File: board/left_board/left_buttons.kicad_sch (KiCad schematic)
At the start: 17 parts, among them SW201 SW_Push, SW202 SW_Push, SW203 SW_Push, SW204 SW_Push, SW205 SW_Push, SW206 SW_Push, SW207 SW_Push, SW208 SW_Push, SW209 SW_Push, SW210 SW_Push, SW211 SW_Push, SW212 SW_Push, SW213 SW_Push

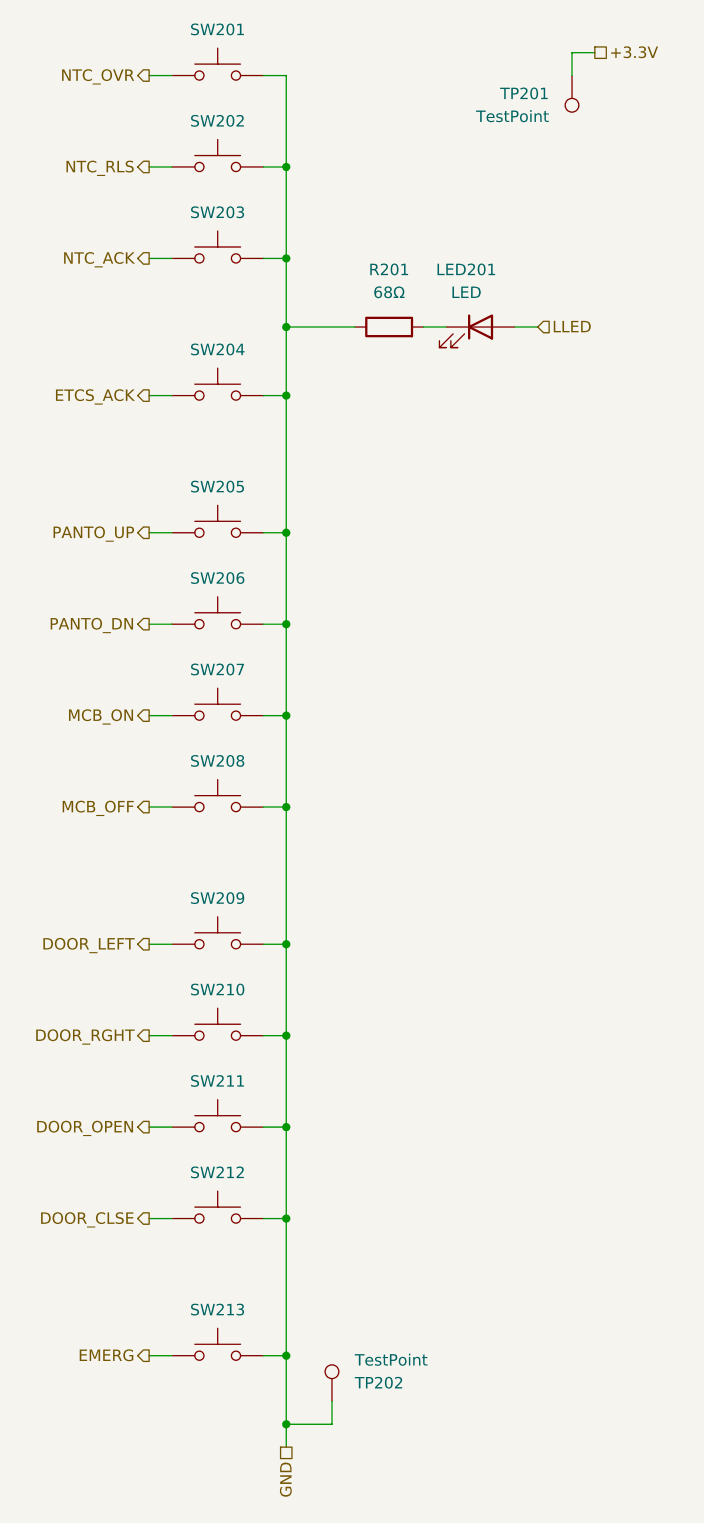
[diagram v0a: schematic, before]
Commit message: add support for pedal
the pedal is mostly envisioned as a secondary dead man's switch input, but
to enable flexible usage, it is wired up to the µC's ADC and supplies
12-bit values for the X axis

things will be set up to cooperate with a Brother-compatible sewing machine
pedal because that's what I have lying around -- those that connect using a
3.5mm TS phone connector, nothing even close to mains voltage
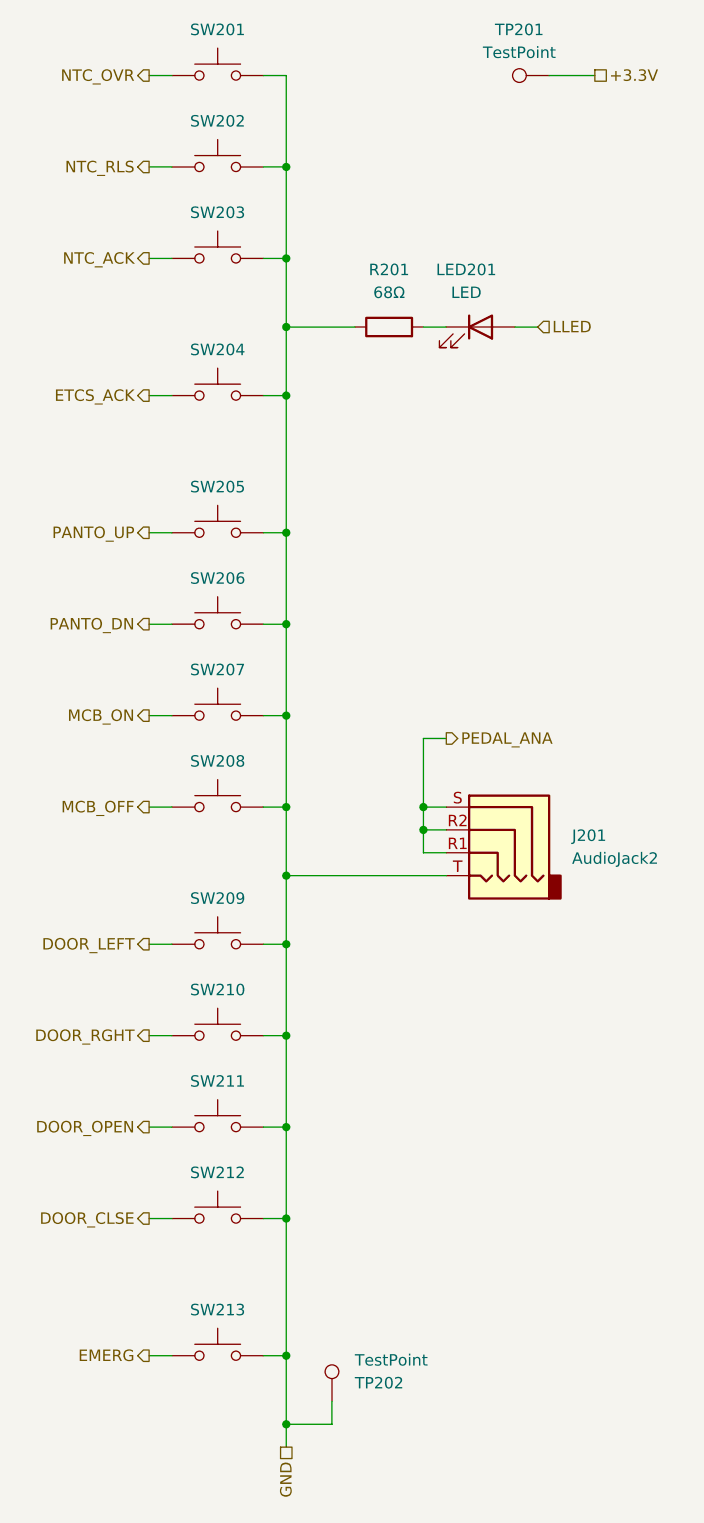
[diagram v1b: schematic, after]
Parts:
- added J201: AudioJack2, Connector_Audio:Jack_3.5mm_PJ320D_Horizontal, symbol Connector_Audio:AudioJack4
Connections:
- net GND: now also J201.T
- new net PEDAL_ANA: J201.R1, J201.R2, J201.S
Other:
- moved on the sheet: TP201
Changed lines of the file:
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@@
+	)
+	(junction
+		(at 74.93 104.14)
+		(diameter 0)
+		(color 0 0 0 0)
+	)
+	(junction
+		(at 74.93 106.68)
+		(diameter 0)
+		(color 0 0 0 0)
 	)
 	(junction
@@
 		(color 0 0 0 0)
 	)
+	(junction
+		(at 59.69 111.76)
+		(diameter 0)
+		(color 0 0 0 0)
+	)
 	(wire
 		(pts
@@
 	(wire
 		(pts
+			(xy 59.69 111.76) (xy 59.69 119.38)
+		)
+		(stroke
+			(width 0)
+			(type default)
+		)
+	)
+	(wire
+		(pts
 			(xy 59.69 22.86) (xy 59.69 33.02)
 		)
@@
 	(wire
 		(pts
+			(xy 74.93 104.14) (xy 74.93 106.68)
+		)
+		(stroke
+			(width 0)
+			(type default)
+		)
+	)
+	(wire
+		(pts
 			(xy 59.69 73.66) (xy 59.69 83.82)
 		)
@@
 	(wire
 		(pts
+			(xy 74.93 104.14) (xy 77.47 104.14)
+		)
+		(stroke
+			(width 0)
+			(type default)
+		)
+	)
+	(wire
+		(pts
 			(xy 57.15 149.86) (xy 59.69 149.86)
 		)
@@
 	(wire
 		(pts
-			(xy 91.44 20.32) (xy 91.44 22.86)
+			(xy 77.47 109.22) (xy 74.93 109.22)
+		)
+		(stroke
+			(width 0)
+			(type default)
+		)
+	)
+	(wire
+		(pts
+			(xy 88.9 22.86) (xy 93.98 22.86)
 		)
 		(stroke
@@
 	(wire
 		(pts
-			(xy 91.44 20.32) (xy 93.98 20.32)
-		)
-		(stroke
-			(width 0)
-			(type default)
-		)
-	)
-	(wire
-		(pts
 			(xy 44.45 73.66) (xy 46.99 73.66)
 		)
@@
 	(wire
 		(pts
+			(xy 74.93 96.52) (xy 77.47 96.52)
+		)
+		(stroke
+			(width 0)
+			(type default)
+		)
+	)
+	(wire
+		(pts
 			(xy 59.69 149.86) (xy 59.69 165.1)
 		)
@@
 	(wire
 		(pts
-			(xy 59.69 104.14) (xy 59.69 119.38)
+			(xy 59.69 104.14) (xy 59.69 111.76)
 		)
 		(stroke
@@
 	(wire
 		(pts
+			(xy 74.93 104.14) (xy 74.93 96.52)
+		)
+		(stroke
+			(width 0)
+			(type default)
+		)
+	)
+	(wire
+		(pts
+			(xy 74.93 106.68) (xy 77.47 106.68)
+		)
+		(stroke
+			(width 0)
+			(type default)
+		)
+	)
+	(wire
+		(pts
 			(xy 57.15 139.7) (xy 59.69 139.7)
 		)
@@
 	(wire
 		(pts
+			(xy 74.93 109.22) (xy 74.93 106.68)
+		)
+		(stroke
+			(width 0)
+			(type default)
+		)
+	)
+	(wire
+		(pts
 			(xy 57.15 58.42) (xy 59.69 58.42)
 		)
@@
 		(pts
 			(xy 59.69 58.42) (xy 59.69 73.66)
+		)
+		(stroke
+			(width 0)
+			(type default)
+		)
+	)
+	(wire
+		(pts
+			(xy 59.69 111.76) (xy 77.47 111.76)
 		)
 		(stroke
@@
 		)
 	)
+	(hierarchical_label "PEDAL_ANA"
+		(shape output)
+		(at 77.47 96.52 0)
+		(fields_autoplaced yes)
+		(effects
+			(font
+				(size 1.27 1.27)
+			)
+			(justify left)
+		)
+	)
 	(hierarchical_label "NTC_RLS"
 		(shape output)
@@
 	(hierarchical_label "+3.3V"
 		(shape passive)
-		(at 93.98 20.32 0)
+		(at 93.98 22.86 0)
 		(fields_autoplaced yes)
 		(effects
@@
 	(symbol
 		(lib_id "Connector:TestPoint")
-		(at 91.44 22.86 0)
+		(at 88.9 22.86 90)
 		(mirror x)
 		(unit 1)
@@
 		(fields_autoplaced yes)
 		(property "Reference" "TP201"
-			(at 88.9 24.8919 0)
-			(effects
-				(font
-					(size 1.27 1.27)
-				)
-				(justify right)
+			(at 85.598 17.78 90)
+			(effects
+				(font
+					(size 1.27 1.27)
+				)
 			)
 		)
 		(property "Value" "TestPoint"
-			(at 88.9 27.4319 0)
-			(effects
-				(font
-					(size 1.27 1.27)
-				)
-				(justify right)
+			(at 85.598 20.32 90)
+			(effects
+				(font
+					(size 1.27 1.27)
+				)
 			)
 		)
 		(property "Footprint" "TestPoint:TestPoint_Pad_D1.0mm"
-			(at 96.52 22.86 0)
+			(at 88.9 27.94 0)
 			(effects
 				(font
@@
 		)
 		(property "Datasheet" "~"
-			(at 96.52 22.86 0)
+			(at 88.9 27.94 0)
 			(effects
 				(font
@@
 		)
 		(property "Description" "test point"
-			(at 91.44 22.86 0)
+			(at 88.9 22.86 0)
 			(effects
 				(font
@@
 					(unit 1)
 				)
+			)
+		)
+	)
+	(symbol
+		(lib_id "Connector_Audio:AudioJack4")
+		(at 82.55 106.68 0)
+		(mirror y)
+		(unit 1)
+		(exclude_from_sim no)
+		(in_bom yes)
+		(on_board yes)
+		(dnp no)
+		(fields_autoplaced yes)
+		(property "Reference" "J201"
+			(at 91.44 107.3149 0)
+			(effects
+				(font
+					(size 1.27 1.27)
+				)
+				(justify right)
+			)
+		)
+		(property "Value" "AudioJack2"
+			(at 91.44 109.8549 0)
+			(effects
+				(font
+					(size 1.27 1.27)
+				)
+				(justify right)
+			)
+		)
+		(property "Footprint" "Connector_Audio:Jack_3.5mm_PJ320D_Horizontal"
+			(at 82.55 106.68 0)
+			(effects
+				(font
+					(size 1.27 1.27)
+				)
+				(hide yes)
+			)
+		)
+		(property "Datasheet" "~"
+			(at 82.55 106.68 0)
+			(effects
+				(font
+					(size 1.27 1.27)
+				)
+				(hide yes)
+			)
+		)
+		(property "Description" "Audio Jack, 4 Poles (TRRS)"
+			(at 82.55 106.68 0)
+			(effects
+				(font
+					(size 1.27 1.27)
+				)
+				(hide yes)
+			)
+		)
+		(property "LCSC" "C431535"
+			(at 82.55 106.68 0)
+			(effects
+				(font
+					(size 1.27 1.27)
+				)
+				(hide yes)
+			)
+		)
+		(pin "S"
+		)
+		(pin "T"
+		)
+		(pin "R2"
+		)
+		(pin "R1"
+		)
+		(instances
+			(project ""
+				(path "/781b8cf7-c5e9-458b-bc5e-9d97c21958eb/ee7ea56d-ccae-4129-b9a8-76b6e32e09cb"
+					(reference "J201")
+					(unit 1)
+				)

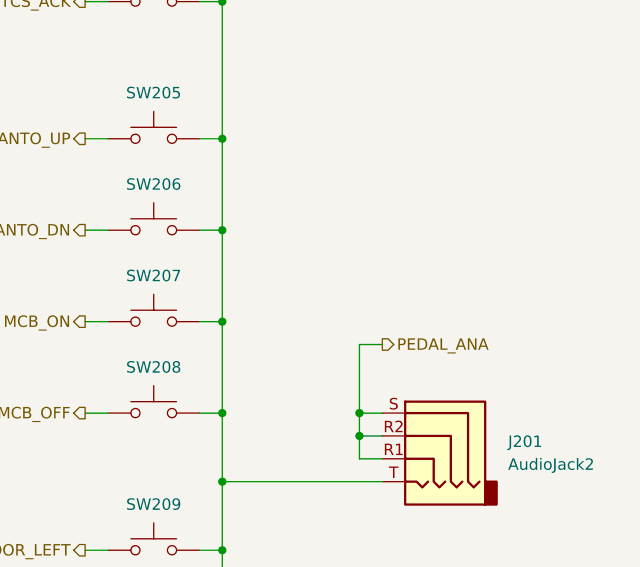
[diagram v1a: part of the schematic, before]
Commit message: left board: pullup resistor for pedal
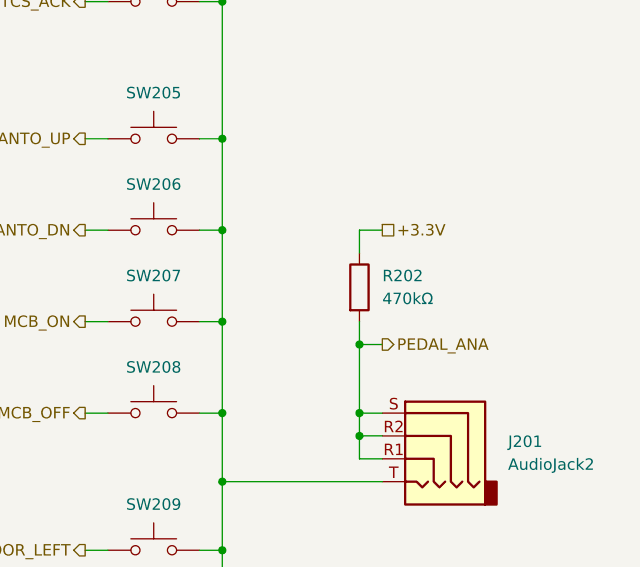
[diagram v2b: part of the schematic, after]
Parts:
- added R202: 470kΩ, Resistor_SMD:R_0603_1608Metric, symbol Device:R
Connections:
- net +3.3V: now also R202.1
- net PEDAL_ANA: now also R202.2
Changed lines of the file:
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@@
+	)
+	(junction
+		(at 74.93 96.52)
+		(diameter 0)
+		(color 0 0 0 0)
 	)
 	(junction
@@
 	(wire
 		(pts
+			(xy 74.93 93.98) (xy 74.93 96.52)
+		)
+		(stroke
+			(width 0)
+			(type default)
+		)
+	)
+	(wire
+		(pts
 			(xy 44.45 73.66) (xy 46.99 73.66)
 		)
@@
 	(wire
 		(pts
+			(xy 74.93 83.82) (xy 77.47 83.82)
+		)
+		(stroke
+			(width 0)
+			(type default)
+		)
+	)
+	(wire
+		(pts
 			(xy 59.69 149.86) (xy 59.69 165.1)
 		)
@@
 		(pts
 			(xy 44.45 33.02) (xy 46.99 33.02)
+		)
+		(stroke
+			(width 0)
+			(type default)
+		)
+	)
+	(wire
+		(pts
+			(xy 74.93 86.36) (xy 74.93 83.82)
 		)
 		(stroke
@@
 			)
 			(justify right)
+		)
+	)
+	(hierarchical_label "+3.3V"
+		(shape passive)
+		(at 77.47 83.82 0)
+		(fields_autoplaced yes)
+		(effects
+			(font
+				(size 1.27 1.27)
+			)
+			(justify left)
 		)
 	)
@@
 					(unit 1)
 				)
+			)
+		)
+	)
+	(symbol
+		(lib_id "Device:R")
+		(at 74.93 90.17 0)
+		(unit 1)
+		(exclude_from_sim no)
+		(in_bom yes)
+		(on_board yes)
+		(dnp no)
+		(fields_autoplaced yes)
+		(property "Reference" "R202"
+			(at 77.47 88.8999 0)
+			(effects
+				(font
+					(size 1.27 1.27)
+				)
+				(justify left)
+			)
+		)
+		(property "Value" "470kΩ"
+			(at 77.47 91.4399 0)
+			(effects
+				(font
+					(size 1.27 1.27)
+				)
+				(justify left)
+			)
+		)
+		(property "Footprint" "Resistor_SMD:R_0603_1608Metric"
+			(at 73.152 90.17 90)
+			(effects
+				(font
+					(size 1.27 1.27)
+				)
+				(hide yes)
+			)
+		)
+		(property "Datasheet" "~"
+			(at 74.93 90.17 0)
+			(effects
+				(font
+					(size 1.27 1.27)
+				)
+				(hide yes)
+			)
+		)
+		(property "Description" "Resistor"
+			(at 74.93 90.17 0)
+			(effects
+				(font
+					(size 1.27 1.27)
+				)
+				(hide yes)
+			)
+		)
+		(property "LCSC" "C23178"
+			(at 74.93 90.17 0)
+			(effects
+				(font
+					(size 1.27 1.27)
+				)
+				(hide yes)
+			)
+		)
+		(pin "2"
+		)
+		(pin "1"
+		)
+		(instances
+			(project ""
+				(path "/781b8cf7-c5e9-458b-bc5e-9d97c21958eb/ee7ea56d-ccae-4129-b9a8-76b6e32e09cb"
+					(reference "R202")
+					(unit 1)
+				)
